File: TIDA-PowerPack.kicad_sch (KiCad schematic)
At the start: 127 parts, among them Q3 IRFH5302TRPBF, Q4 IRFH5302TRPBF, SW1 SS-12M11G5, U1 TPS25750DRJKR, U10 XT30PW-F, U15 SB1045L_C2844167, U17 SMTSO3015CTJ, U18 SMTSO3015CTJ, U19 SMTSO3015CTJ, U2 CAT24C256WI-GT3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

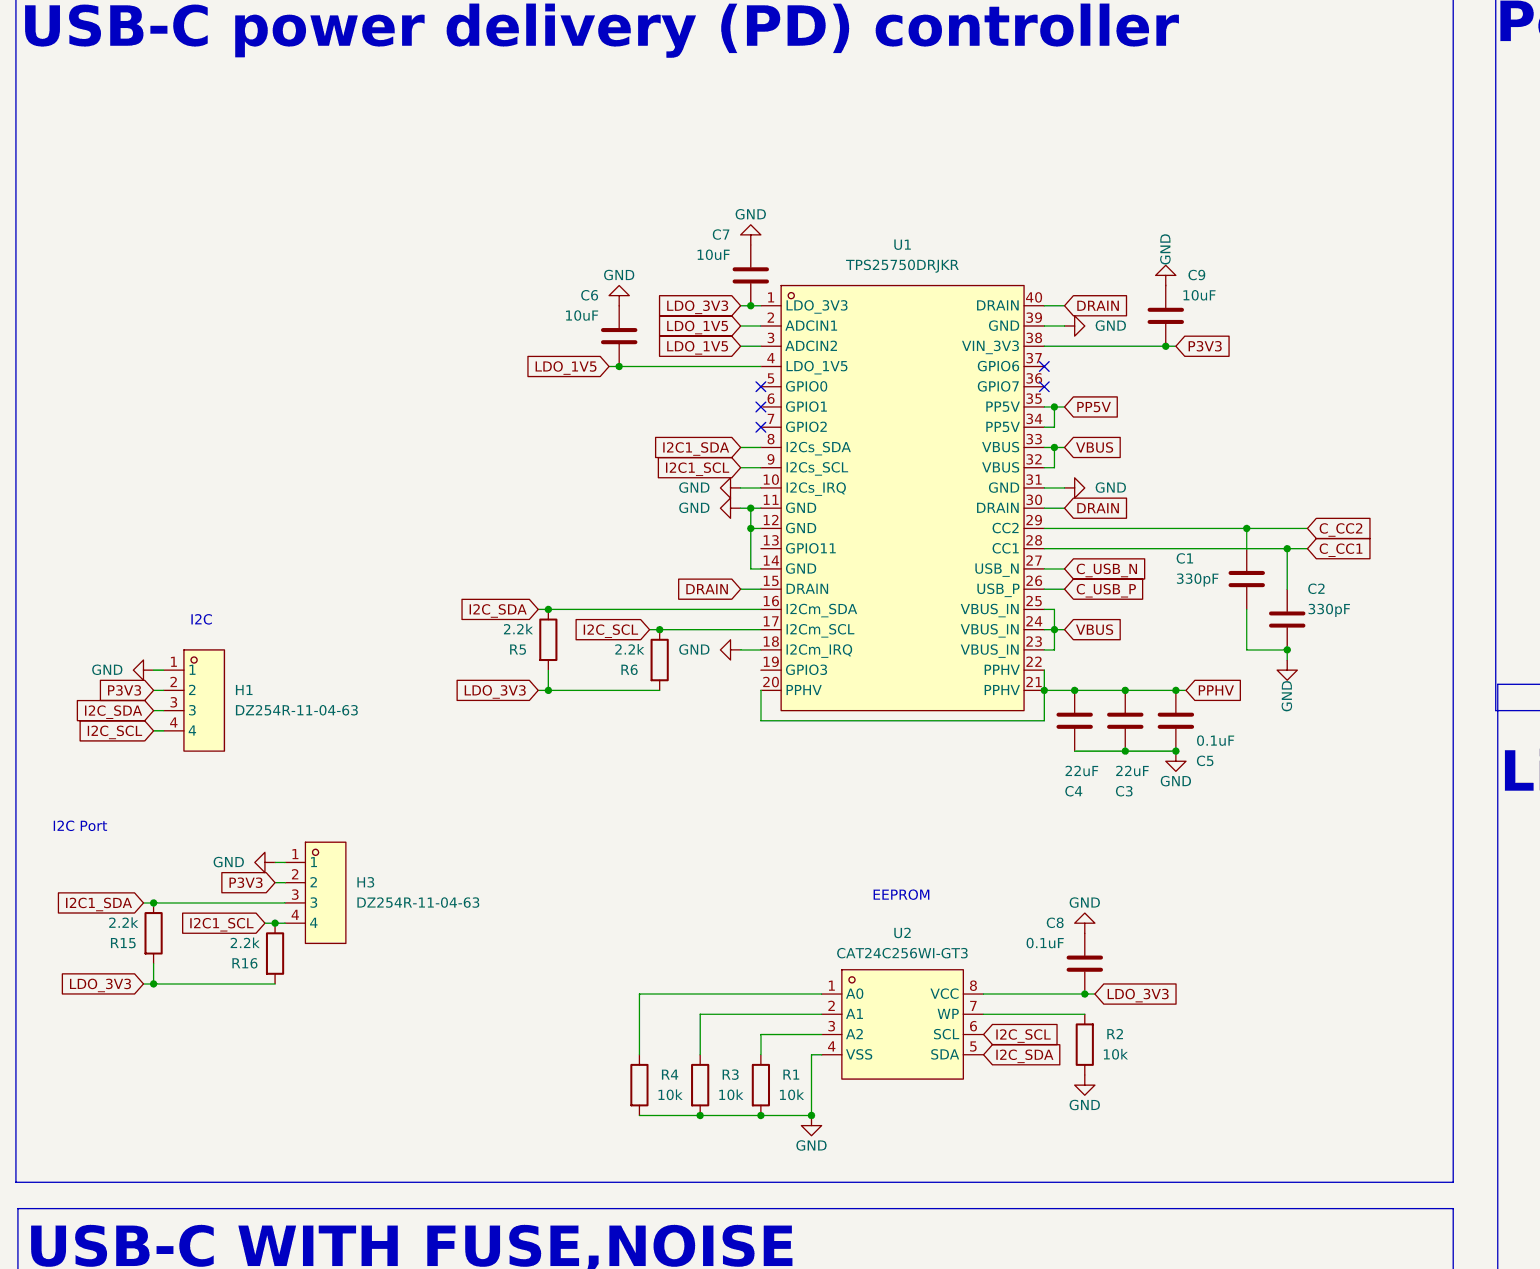
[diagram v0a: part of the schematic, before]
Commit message: replace TPS25750D with TPS25751 chip
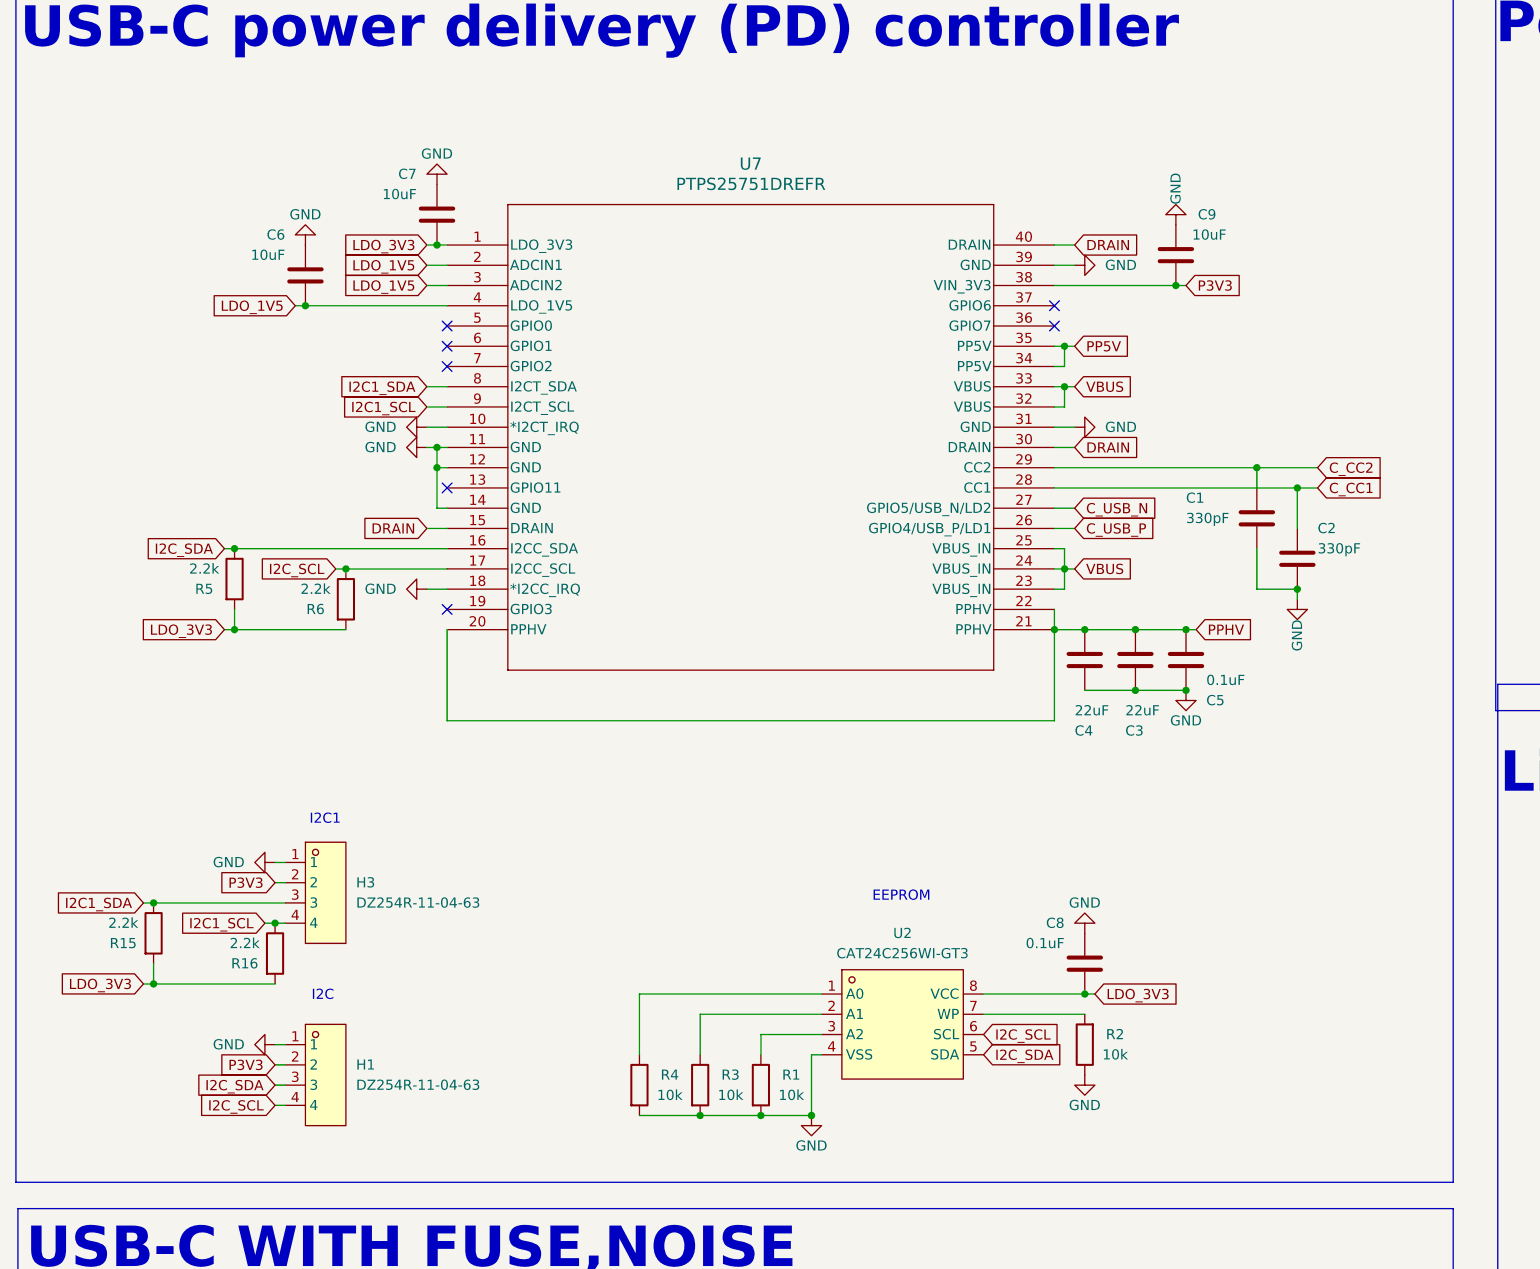
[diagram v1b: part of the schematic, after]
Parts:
- removed U1: TPS25750DRJKR, easyeda2kicad:QFN-38_L6.0-W4.0-P0.40-TL-EP_RJK, symbol easyeda2kicad:TPS25750DRJKR
- added U7: PTPS25751DREFR, TPS25751DREFR:WQFN38_REF_TEX, symbol TPS25751DREFR:PTPS25751DREFR
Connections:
- net C_CC1: now also U7.28 (CC1)
- net C_CC2: now also U7.29 (CC2)
- net C_USB_N: now also U7.27 (GPIO5/USB_N/LD2)
- net C_USB_P: now also U7.26 (GPIO4/USB_P/LD1)
- net DRAIN: now also U7.15 (DRAIN), U7.30 (DRAIN), U7.40 (DRAIN)
- net GND: now also U7.10 (*I2CT_IRQ), U7.11 (GND), U7.12 (GND), U7.14 (GND), U7.18 (*I2CC_IRQ), U7.31 (GND), U7.39 (GND)
- net I2C1_SCL: now also U7.9 (I2CT_SCL)
- net I2C1_SDA: now also U7.8 (I2CT_SDA)
- net I2C_SCL: now also U7.17 (I2CC_SCL)
- net I2C_SDA: now also U7.16 (I2CC_SDA)
- net LDO_1V5: now also U7.2 (ADCIN1), U7.3 (ADCIN2), U7.4 (LDO_1V5)
- net LDO_3V3: now also U7.1 (LDO_3V3)
- net P3V3: now also U7.38 (VIN_3V3)
- net PP5V: now also U7.34 (PP5V), U7.35 (PP5V)
- net PPHV: now also U7.20 (PPHV), U7.21 (PPHV), U7.22 (PPHV)
- net VBUS: now also U7.23 (VBUS_IN), U7.24 (VBUS_IN), U7.25 (VBUS_IN), U7.32 (VBUS), U7.33 (VBUS)
- no-connect marks 11 -> 13
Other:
- note added: "I2C1"
- note removed: "I2C Port"
- moved on the sheet: C1, C2, C3, C4, C5, C6, C7, C9, H1, R5, R6
